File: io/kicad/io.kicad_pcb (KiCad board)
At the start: 2 copper layers, 90 x 88.4 mm, 117 parts, among them J1 Conn_01x07_Pin, J2 Conn_01x02_Pin, J3 Conn_01x02_Pin, J4 Conn_01x02_Pin, J5 pcie_98, U1 ADS1261BIRHBT, U2 ESD5344D-TP, U3 TPS7A2050PDBVR, U4 TPS7A2025PDBVRr, U6 TPS65135, U7 ADP7182AUJZ-5.0, U8 ADP7182AUJZ-2.5, U9 XC6206P332MR

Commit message: Renamed the fork of kicad adc to 'io'.
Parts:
- J1: footprint adc:connector_7pins_horizontal -> io:connector_7pins_horizontal
- J2, J3, J4: footprint adc:connector_2pins_horizontal -> io:connector_2pins_horizontal
- L1: footprint adc:Inductor_C329578 -> io:Inductor_C329578
- U1: footprint adc:RHB0032E -> io:RHB0032E
- U3, U4: footprint adc:SOT-23-5 -> io:SOT-23-5
- U6: footprint adc:WQFN-16-1EP_3x3mm_P0.5mm_EP1.68x1.68mm_ThermalVias -> io:WQFN-16-1EP_3x3mm_P0.5mm_EP1.68x1.68mm_ThermalVias

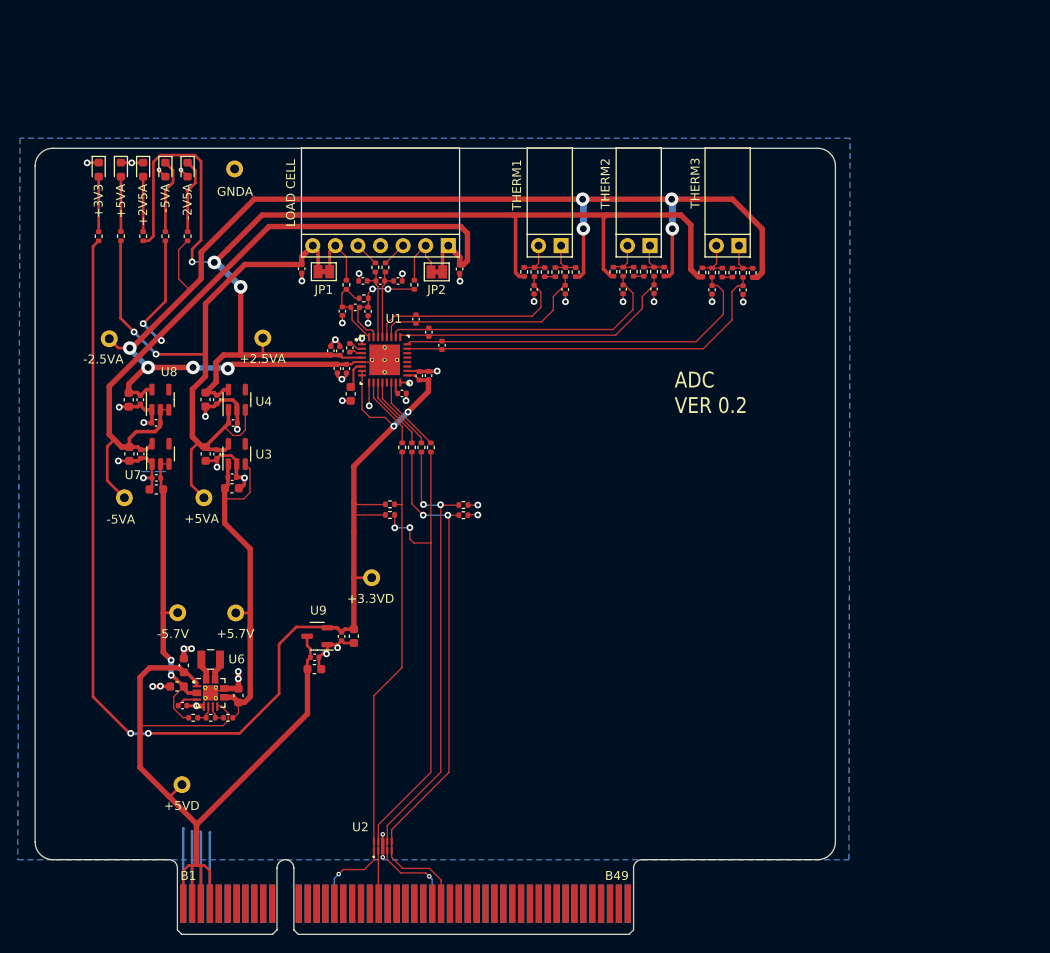
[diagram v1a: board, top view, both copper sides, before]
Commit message: Cleaned out the io kicad from adc leftovers.
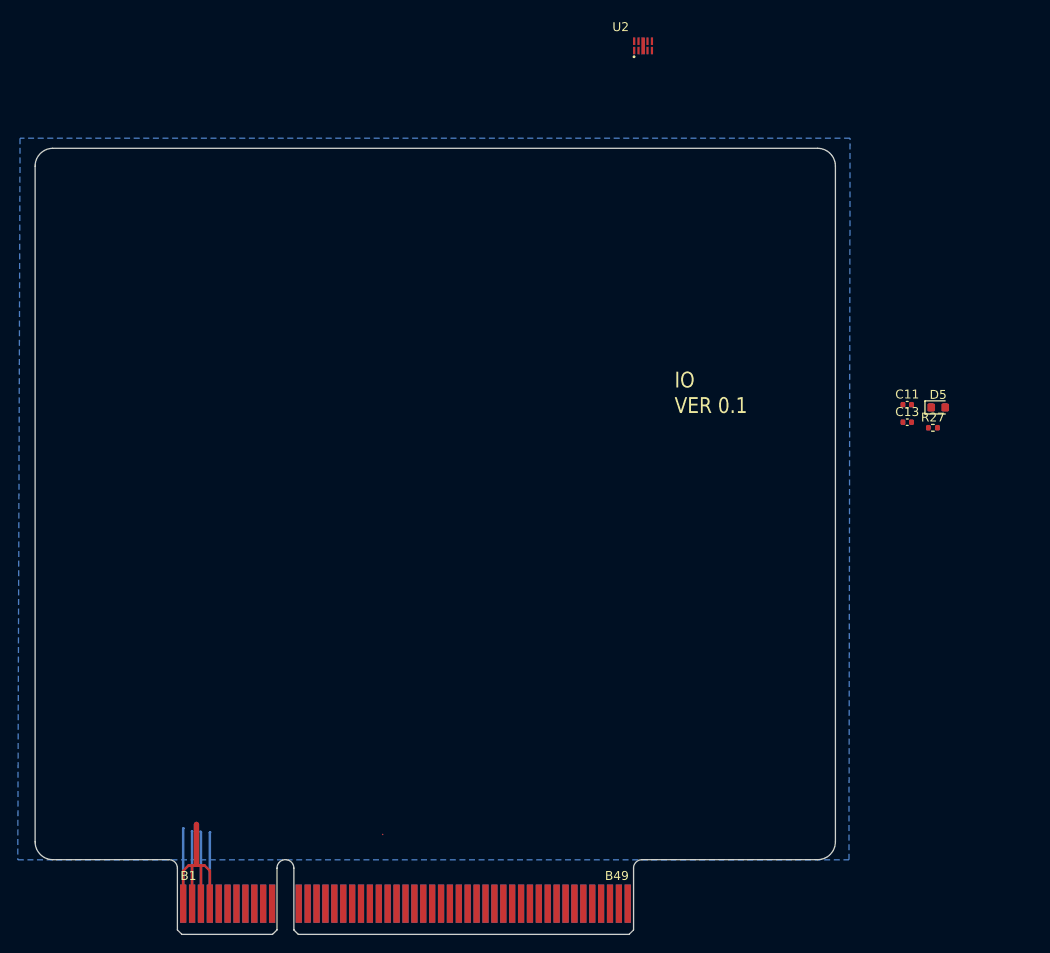
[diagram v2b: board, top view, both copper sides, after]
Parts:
- removed C1, C5, C6: 2u2, Capacitor_SMD:C_0402_1005Metric
- removed C10, C21, C35, C45, C46: 1u, Capacitor_SMD:C_0402_1005Metric
- removed C12, C2, C23, C24, C25, C27, C3, C30, C31, C34, C36, C38, C39, C4, C43, C44, C7, C8, C9: 100n, Capacitor_SMD:C_0402_1005Metric
- removed C14, C16, C18, C20: 22n, Capacitor_SMD:C_0402_1005Metric
- removed C15, C19: 220n, Capacitor_SMD:C_0402_1005Metric
- removed C17: 4n7, Capacitor_SMD:C_0402_1005Metric
- removed C22, C26, C28, C29, C32, C33, C37, C40, C41, C42, C47, C48: 10u, Capacitor_SMD:C_0603_1608Metric
- removed D1, D2, D3, D4: GRN, LED_SMD:LED_0603_1608Metric
- removed J1: Conn_01x07_Pin, io:connector_7pins_horizontal
- removed J2, J3, J4: Conn_01x02_Pin, io:connector_2pins_horizontal
- removed JP1, JP2: SolderJumper_2_Bridged, Jumper:SolderJumper-2_P1.3mm_Bridged_Pad1.0x1.5mm
- removed L1: 2u2H, io:Inductor_C329578
- removed R1, R12, R13, R2, R3, R30, R36, R37, R38, R39, R40, R41, R42, R7, R8: 2K 0.1%, Resistor_SMD:R_0402_1005Metric
- removed R10, R11, R20, R34, R4, R5, R6, R9: 1K, Resistor_SMD:R_0402_1005Metric
- removed R15, R16, R28, R29: 51K, Resistor_SMD:R_0402_1005Metric
- removed R18, R19, R21, R22: 47R, Resistor_SMD:R_0402_1005Metric
- removed R23, R24: 10K, Resistor_SMD:R_0402_1005Metric
- removed R25, R26: 5K1, Resistor_SMD:R_0402_1005Metric
- removed R31: 360K 1%, Resistor_SMD:R_0402_1005Metric
- removed R32: 100K 1%, Resistor_SMD:R_0402_1005Metric
- removed R33: 464K 1%, Resistor_SMD:R_0402_1005Metric
- removed TP1, TP2, TP3, TP4, TP5, TP6, TP7, TP8, TP9: TestPoint, common:Test_Pad
- removed U1: ADS1261BIRHBT, io:RHB0032E
- removed U3: TPS7A2050PDBVR, io:SOT-23-5
- removed U4: TPS7A2025PDBVRr, io:SOT-23-5
- removed U6: TPS65135, io:WQFN-16-1EP_3x3mm_P0.5mm_EP1.68x1.68mm_ThermalVias
- removed U7: ADP7182AUJZ-5.0, Package_TO_SOT_SMD:TSOT-23-5
- removed U8: ADP7182AUJZ-2.5, Package_TO_SOT_SMD:TSOT-23-5
- removed U9: XC6206P332MR, Package_TO_SOT_SMD:SOT-23-3
- moved D5 98.1 mm to (73.4, -59.3), turned to 0 degrees
- moved R27 96.3 mm to (72.8, -57.0), turned to 0 degrees
- moved U2 94.6 mm to (40.2, -99.9)
- moved C13 55.1 mm to (69.9, -57.6), turned to 0 degrees
- moved C11 53.9 mm to (69.9, -59.6), turned to 0 degrees
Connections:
- C11 pad 1: /+3V3D -> unconnected-(C11-Pad1)
- C11 pad 2: GND -> unconnected-(C11-Pad2)
- C13 pad 1: /+3V3D -> unconnected-(C13-Pad1)
- C13 pad 2: GND -> unconnected-(C13-Pad2)
- D5 pad 1: GND -> unconnected-(D5-K-Pad1)
- D5 pad 2: Net-(D5-A) -> unconnected-(D5-A-Pad2)
- R27 pad 1: /+3V3D -> unconnected-(R27-Pad1)
- R27 pad 2: Net-(D5-A) -> unconnected-(R27-Pad2)
- U2 pad 1: /PB14 -> unconnected-(U2-D1-Pad1)
- U2 pad 2: /PA6 -> unconnected-(U2-D2-Pad2)
- U2 pad 3: GND -> unconnected-(U2-GND-Pad3)
- U2 pad 4: /PA7 -> unconnected-(U2-D3-Pad4)
- U2 pad 5: /PA5 -> unconnected-(U2-D4-Pad5)
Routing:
- net /-2V5A: track 151.7 -> 0.00 mm, vias 8 -> 0
- net /+2V5A: track 145.5 -> 0.00 mm, vias 3 -> 0
- net /+3V3D: track 142.6 -> 0.00 mm, vias 4 -> 0
- net /-5VA: track 99.1 -> 0.00 mm, vias 2 -> 0
- net GND: track 121.2 -> 32.8 mm, vias 45 -> 0
- net /+5VA: track 76.4 -> 0.00 mm, vias 2 -> 0
- net +5VD: track 93.2 -> 24.9 mm
- net /PA5: track 62.3 -> 0.00 mm, vias 2 -> 0
- net /PA7: track 60.7 -> 0.00 mm, vias 3 -> 0
- net /PA6: track 60.2 -> 0.07 mm, vias 2 -> 0
- net /PB14: track 56.2 -> 0.00 mm, vias 1 -> 0
- net /AIN9: track 43.5 -> 0.00 mm
- net /AIN8: track 42.0 -> 0.00 mm
- net /+5V7: track 41.4 -> 0.00 mm
- net /-5V7: track 36.1 -> 0.00 mm, vias 2 -> 0
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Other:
- board text added: "IO VER 0.1"
- board text removed: "+2.5VA"
- board text removed: "+2V5A"
- board text removed: "+3.3VD"
- board text removed: "+3V3"
- board text removed: "+5.7V"
- board text removed: "+5VA"
- board text removed: "+5VD"
- board text removed: "-2.5VA"
- board text removed: "-2V5A"
- board text removed: "-5.7V"
- board text removed: "-5VA"
- board text removed: "ADC VER 0.2"
- board text removed: "GNDA"
- board text removed: "LOAD CELL"
- board text removed: "THERM1"
- board text removed: "THERM2"
- board text removed: "THERM3"

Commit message: IO board schematic is feature complete.
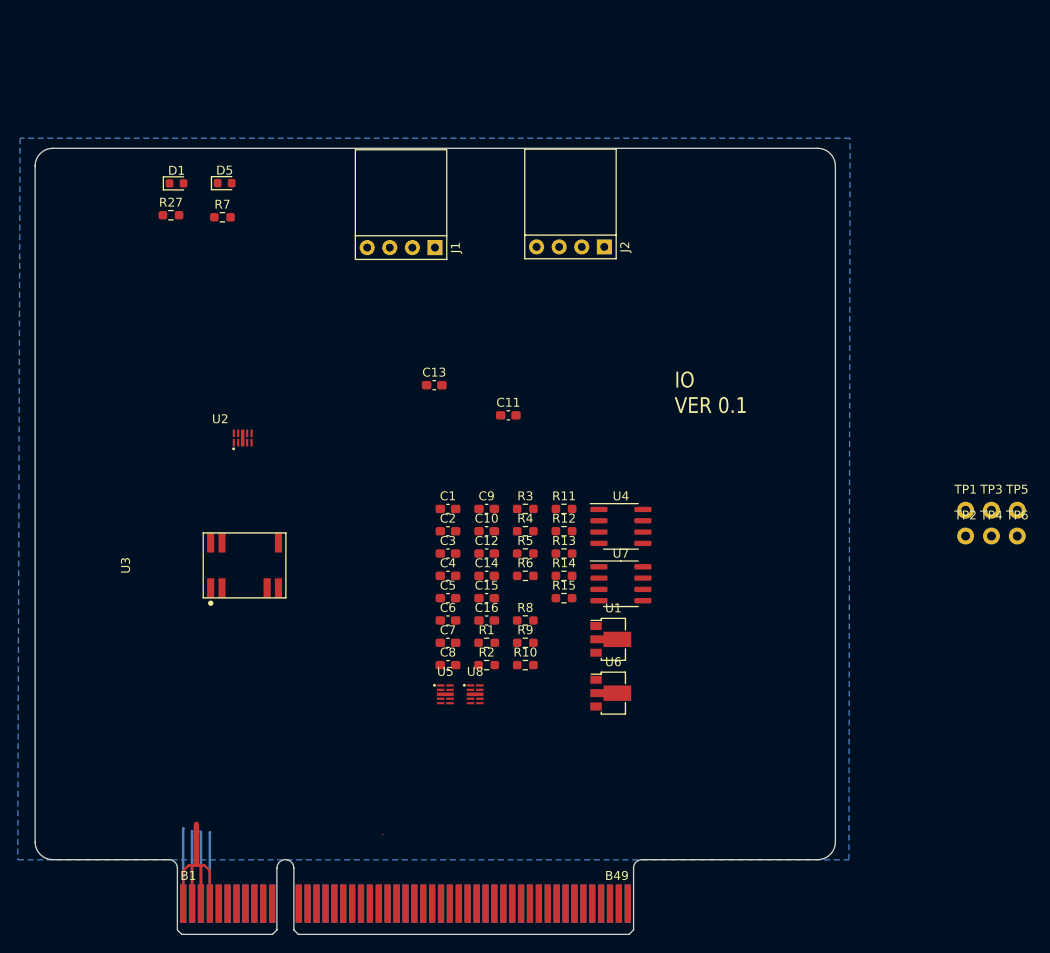
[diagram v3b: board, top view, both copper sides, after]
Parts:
- added C1: 10u, Capacitor_SMD:C_0603_1608Metric_Pad1.08x0.95mm_HandSolder, F.Cu at (18.3, -47.8)
- added C10: 1u, Capacitor_SMD:C_0603_1608Metric_Pad1.08x0.95mm_HandSolder, F.Cu at (22.6, -45.3)
- added C12: 100n, Capacitor_SMD:C_0603_1608Metric_Pad1.08x0.95mm_HandSolder, F.Cu at (22.6, -42.8)
- added C14: 1u, Capacitor_SMD:C_0603_1608Metric_Pad1.08x0.95mm_HandSolder, F.Cu at (22.6, -40.3)
- added C15: 100n, Capacitor_SMD:C_0603_1608Metric_Pad1.08x0.95mm_HandSolder, F.Cu at (22.6, -37.8)
- added C16: 100n, Capacitor_SMD:C_0603_1608Metric_Pad1.08x0.95mm_HandSolder, F.Cu at (22.6, -35.3)
- added C2: 100n, Capacitor_SMD:C_0603_1608Metric_Pad1.08x0.95mm_HandSolder, F.Cu at (18.3, -45.3)
- added C3: 10u, Capacitor_SMD:C_0603_1608Metric_Pad1.08x0.95mm_HandSolder, F.Cu at (18.3, -42.8)
- added C4: 10u, Capacitor_SMD:C_0603_1608Metric_Pad1.08x0.95mm_HandSolder, F.Cu at (18.3, -40.3)
- added C5: 100n, Capacitor_SMD:C_0603_1608Metric_Pad1.08x0.95mm_HandSolder, F.Cu at (18.3, -37.8)
- added C6: 100n, Capacitor_SMD:C_0603_1608Metric_Pad1.08x0.95mm_HandSolder, F.Cu at (18.3, -35.3)
- added C7: 100n, Capacitor_SMD:C_0603_1608Metric_Pad1.08x0.95mm_HandSolder, F.Cu at (18.3, -32.8)
- added C8: 10u, Capacitor_SMD:C_0603_1608Metric_Pad1.08x0.95mm_HandSolder, F.Cu at (18.3, -30.3)
- added C9: 10u, Capacitor_SMD:C_0603_1608Metric_Pad1.08x0.95mm_HandSolder, F.Cu at (22.6, -47.8)
- added D1: GRN, LED_SMD:LED_0603_1608Metric, F.Cu at (-12.2, -84.5)
- added J1: Conn_01x04_Pin, common:connector_4pins_horizontal, F.Cu at (13.0, -77.2)
- added J2: Conn_01x04_Pin, common:connector_4pins_horizontal, F.Cu at (32.1, -77.3)
- added R1: 1K, Resistor_SMD:R_0603_1608Metric_Pad0.98x0.95mm_HandSolder, F.Cu at (22.6, -32.8)
- added R10: 0R, Resistor_SMD:R_0603_1608Metric_Pad0.98x0.95mm_HandSolder, F.Cu at (27.0, -30.3)
- added R11: 24K, Resistor_SMD:R_0603_1608Metric_Pad0.98x0.95mm_HandSolder, F.Cu at (31.3, -47.8)
- added R12: 1K, Resistor_SMD:R_0603_1608Metric_Pad0.98x0.95mm_HandSolder, F.Cu at (31.3, -45.3)
- added R13: 0R, Resistor_SMD:R_0603_1608Metric_Pad0.98x0.95mm_HandSolder, F.Cu at (31.3, -42.8)
- added R14: 1K, Resistor_SMD:R_0603_1608Metric_Pad0.98x0.95mm_HandSolder, F.Cu at (31.3, -40.3)
- added R15: 24K, Resistor_SMD:R_0603_1608Metric_Pad0.98x0.95mm_HandSolder, F.Cu at (31.3, -37.8)
- added R2: 1K, Resistor_SMD:R_0603_1608Metric_Pad0.98x0.95mm_HandSolder, F.Cu at (22.6, -30.3)
- added R3: 0R, Resistor_SMD:R_0603_1608Metric_Pad0.98x0.95mm_HandSolder, F.Cu at (27.0, -47.8)
- added R4: 24K, Resistor_SMD:R_0603_1608Metric_Pad0.98x0.95mm_HandSolder, F.Cu at (27.0, -45.3)
- added R5: 0R, Resistor_SMD:R_0603_1608Metric_Pad0.98x0.95mm_HandSolder, F.Cu at (27.0, -42.8)
- added R6: 0R, Resistor_SMD:R_0603_1608Metric_Pad0.98x0.95mm_HandSolder, F.Cu at (27.0, -40.3)
- added R7: 5K1, Resistor_SMD:R_0603_1608Metric_Pad0.98x0.95mm_HandSolder, F.Cu at (-7.08, -80.6)
- added R8: 24K, Resistor_SMD:R_0603_1608Metric_Pad0.98x0.95mm_HandSolder, F.Cu at (27.0, -35.3)
- added R9: 0R, Resistor_SMD:R_0603_1608Metric_Pad0.98x0.95mm_HandSolder, F.Cu at (27.0, -32.8)
- added TP1: TestPoint, common:Test_Pad, F.Cu at (76.5, -47.7)
- added TP2: TestPoint, common:Test_Pad, F.Cu at (76.5, -44.8)
- added TP3: TestPoint, common:Test_Pad, F.Cu at (79.4, -47.7)
- added TP4: TestPoint, common:Test_Pad, F.Cu at (79.4, -44.8)
- added TP5: TestPoint, common:Test_Pad, F.Cu at (82.3, -47.7)
- added TP6: TestPoint, common:Test_Pad, F.Cu at (82.3, -44.8)
- added U1: XC6206P332MR, Package_TO_SOT_SMD:SOT-89-3, F.Cu at (36.9, -33.2)
- added U3: B0505MT-1WR4, io:Converter_DCDC, F.Cu at (-4.60, -41.5)
- added U4: ADUM1201ARZ-RL7, Package_SO:SOIC-8_3.9x4.9mm_P1.27mm, F.Cu at (37.7, -45.9)
- added U5: ESD5344D-TP, common:Diodes_UDFN-10_1.0x2.5mm_P0.5mm, F.Cu at (18.0, -27.0)
- added U6: XC6206P332MR, Package_TO_SOT_SMD:SOT-89-3, F.Cu at (36.9, -27.1)
- added U7: ADUM1201ARZ-RL7, Package_SO:SOIC-8_3.9x4.9mm_P1.27mm, F.Cu at (37.7, -39.4)
- added U8: ESD5344D-TP, common:Diodes_UDFN-10_1.0x2.5mm_P0.5mm, F.Cu at (21.3, -27.0)
- C11: value 1u -> 100n; footprint Capacitor_SMD:C_0402_1005Metric -> Capacitor_SMD:C_0603_1608Metric_Pad1.08x0.95mm_HandSolder
- C13: footprint Capacitor_SMD:C_0402_1005Metric -> Capacitor_SMD:C_0603_1608Metric_Pad1.08x0.95mm_HandSolder
- R27: footprint Resistor_SMD:R_0402_1005Metric -> Resistor_SMD:R_0603_1608Metric_Pad0.98x0.95mm_HandSolder
- moved R27 89.0 mm to (-12.9, -80.9)
- moved D5 84.1 mm to (-6.83, -84.5)
- moved U2 63.0 mm to (-4.81, -55.8)
- moved C13 53.4 mm to (16.7, -61.8)
- moved C11 44.9 mm to (25.1, -58.4)
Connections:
- net +5VD renamed +5V
- C11 pad 1: unconnected-(C11-Pad1) -> GND
- C11 pad 2: unconnected-(C11-Pad2) -> +3.3V
- C13 pad 1: unconnected-(C13-Pad1) -> GND1
- C13 pad 2: unconnected-(C13-Pad2) -> /+5VF
- D5 pad 1: unconnected-(D5-K-Pad1) -> GND1
- D5 pad 2: unconnected-(D5-A-Pad2) -> Net-(D5-A)
- J5 pad A14: unconnected-(J5-Pin_a14-PadA14) -> /PC6
- J5 pad A16: /PB14 -> unconnected-(J5-Pin_a16-PadA16)
- J5 pad A21: unconnected-(J5-Pin_a21-PadA21) -> /PA2
- J5 pad A27: /PA7 -> unconnected-(J5-Pin_a27-PadA27)
- J5 pad B21: /PA6 -> unconnected-(J5-Pin_b21-PadB21)
- J5 pad B27: unconnected-(J5-Pin_b27-PadB27) -> /PA3
- J5 pad B28: /PA5 -> unconnected-(J5-Pin_b28-PadB28)
- J5 pad B7: unconnected-(J5-Pin_b7-PadB7) -> /PC7
- R27 pad 1: unconnected-(R27-Pad1) -> /+3V3F
- R27 pad 2: unconnected-(R27-Pad2) -> Net-(D5-A)
- U2 pad 1: unconnected-(U2-D1-Pad1) -> Net-(J1-Pin_4)
- U2 pad 2: unconnected-(U2-D2-Pad2) -> Net-(U2-D2)
- U2 pad 3: unconnected-(U2-GND-Pad3) -> GND1
- U2 pad 4: unconnected-(U2-D3-Pad4) -> Net-(U2-D3)

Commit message: Work in progress. Placement of the IO board.
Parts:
- moved R10 47.1 mm to (3.76, -73.5), turned to -90 degrees
- moved R6 46.8 mm to (0.00, -73.5), turned to -90 degrees
- moved C8 46.3 mm to (-0.33, -18.7)
- moved U6 46.3 mm to (-9.23, -36.9)
- moved R9 44.1 mm to (5.79, -73.5), turned to -90 degrees
- moved U2 41.1 mm to (35.4, -65.6)
- moved R11 40.4 mm to (38.7, -71.4)
- moved C1 39.3 mm to (-17.2, -23.3)
- moved C10 39.1 mm to (42.6, -68.9)
- moved C2 38.2 mm to (-15.4, -19.9)
- moved U5 38.1 mm to (5.18, -65.6), turned to -90 degrees
- moved R2 35.8 mm to (2.03, -73.5), turned to 90 degrees
- moved R12 34.5 mm to (-4.75, -56.4), turned to -90 degrees
- moved R13 34.4 mm to (38.9, -62.5)
- moved R4 34.2 mm to (7.62, -73.5), turned to -90 degrees
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- renumbered C4 to C1, C16 to C10, C3 to C12, C9 to C13, C6 to C14, C7 to C15, C8 to C16, C5 to C2, C14 to C3, C10 to C4, C1 to C5, C15 to C6, C12 to C7, C13 to C8, C2 to C9, D5 to D1, D1 to D2, J2 to J1, J1 to J2, J5 to J3, R13 to R1, R2 to R10, R9 to R11, R5 to R12, R10 to R13, R6 to R14, R27 to R15, R7 to R16, R3 to R2, R11 to R3, R15 to R5, R8 to R6, R12 to R7, R14 to R8, R1 to R9, TP3 to TP1, TP4 to TP2, TP5 to TP3, TP6 to TP4, TP1 to TP5, TP2 to TP6, U3 to U1, U8 to U2, U2 to U3, U7 to U4, U4 to U5, U1 to U6, U6 to U7, U5 to U8
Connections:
- C3 pad 2: Net-(J2-Pin_4) -> Net-(J1-Pin_1)
- C4 pad 2: Net-(J1-Pin_4) -> Net-(J2-Pin_1)
- C6 pad 2: Net-(J2-Pin_4) -> Net-(J1-Pin_1)
- C7 pad 2: Net-(J1-Pin_4) -> Net-(J2-Pin_1)
- J1 pad 1: GND1 -> Net-(J1-Pin_1)
- J1 pad 2: Net-(J2-Pin_2) -> Net-(J1-Pin_2)
- J1 pad 3: Net-(J2-Pin_3) -> Net-(J1-Pin_3)
- J1 pad 4: Net-(J2-Pin_4) -> GND1
- J2 pad 1: GND1 -> Net-(J2-Pin_1)
- J2 pad 2: Net-(J1-Pin_2) -> Net-(J2-Pin_2)
- J2 pad 3: Net-(J1-Pin_3) -> Net-(J2-Pin_3)
- J2 pad 4: Net-(J1-Pin_4) -> GND1
- R1 pad 2: Net-(J2-Pin_2) -> Net-(J1-Pin_3)
- R11 pad 1: Net-(J2-Pin_4) -> Net-(J1-Pin_1)
- R12 pad 1: Net-(J1-Pin_4) -> Net-(J2-Pin_1)
- R13 pad 1: Net-(J2-Pin_4) -> Net-(J1-Pin_1)
- R14 pad 1: Net-(J1-Pin_4) -> Net-(J2-Pin_1)
- R2 pad 2: Net-(J1-Pin_2) -> Net-(J2-Pin_3)
- R3 pad 2: Net-(J2-Pin_4) -> Net-(J1-Pin_1)
- R4 pad 2: Net-(J1-Pin_4) -> Net-(J2-Pin_1)
- R7 pad 1: Net-(J2-Pin_3) -> Net-(J1-Pin_2)
- R9 pad 1: Net-(J1-Pin_3) -> Net-(J2-Pin_2)
- U2 pad 1: Net-(J2-Pin_4) -> Net-(J1-Pin_1)
- U3 pad 1: Net-(J1-Pin_4) -> Net-(J2-Pin_1)
- U4 pad 1: Net-(J2-Pin_4) -> Net-(J1-Pin_1)
- U5 pad 1: Net-(J1-Pin_4) -> Net-(J2-Pin_1)
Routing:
- net /PA2: track 0.00 -> 68.8 mm, vias 0 -> 3
- net /PA3: track 0.00 -> 67.5 mm
- net Net-(J2-Pin_1): track 0.00 -> 27.8 mm
- net /PC7: track 0.00 -> 20.3 mm
- net /PC6: track 0.00 -> 13.7 mm, vias 0 -> 1
- net +3.3V: track 0.00 -> 12.9 mm
- net /+3V3F: track 0.00 -> 12.8 mm
- net GND1: track 0.00 -> 10.5 mm, vias 0 -> 3
- net Net-(R10-Pad1): track 0.00 -> 9.36 mm
- net GND: track 32.8 -> 41.3 mm, vias 0 -> 3
- net /+5VF: track 0.00 -> 5.81 mm
- net Net-(U3-D3): track 0.00 -> 5.24 mm
- net Net-(U3-D2): track 0.00 -> 5.05 mm
- net Net-(J2-Pin_3): track 0.00 -> 3.58 mm
- net Net-(D1-A): track 0.00 -> 3.55 mm
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- added copper zone on B.Cu, net GND1
